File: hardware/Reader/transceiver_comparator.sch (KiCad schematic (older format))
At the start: 12 parts

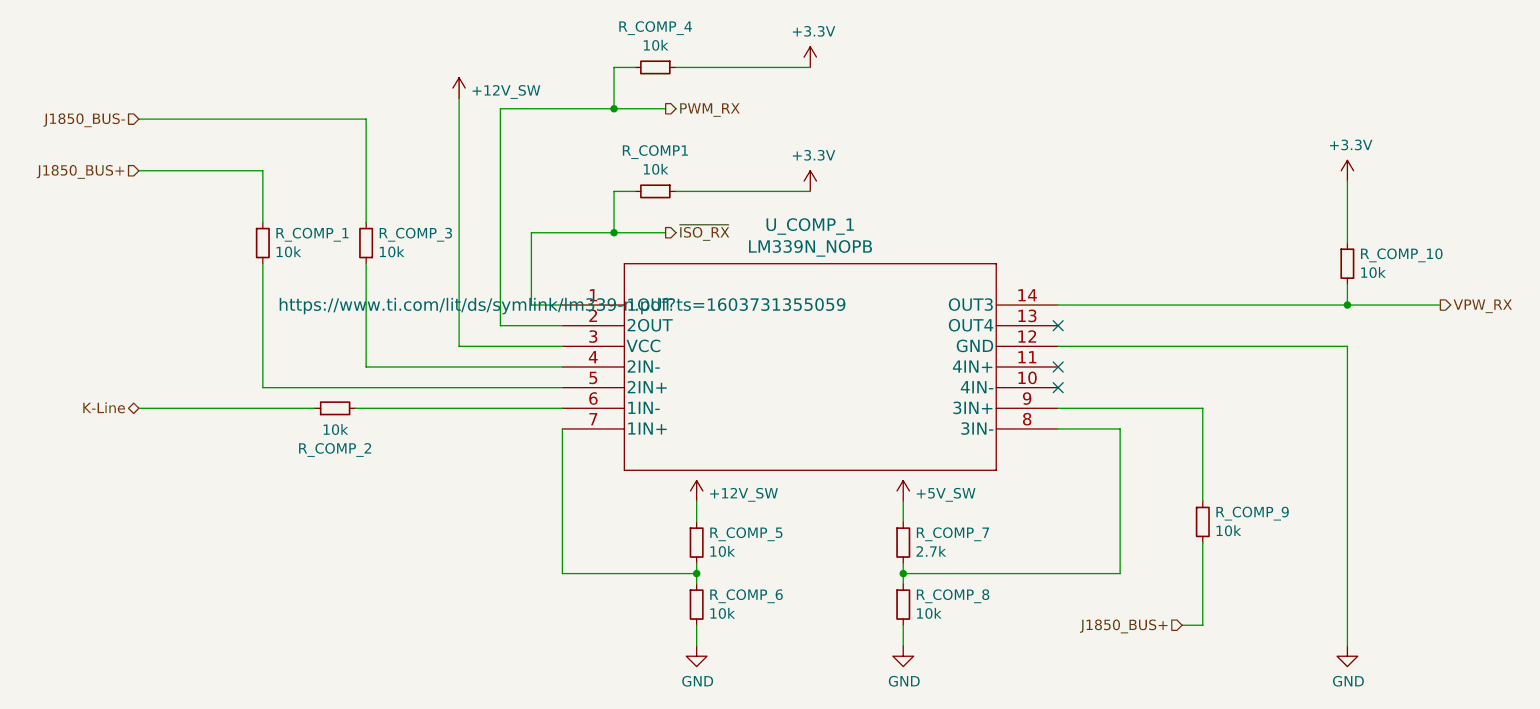
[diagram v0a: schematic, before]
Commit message: Updated reader schematic to v0.0.5 by adding ESP32, removing unused transceivers, fixed design flaws, increased header pins and fixed footprints. Working on reader PCB design
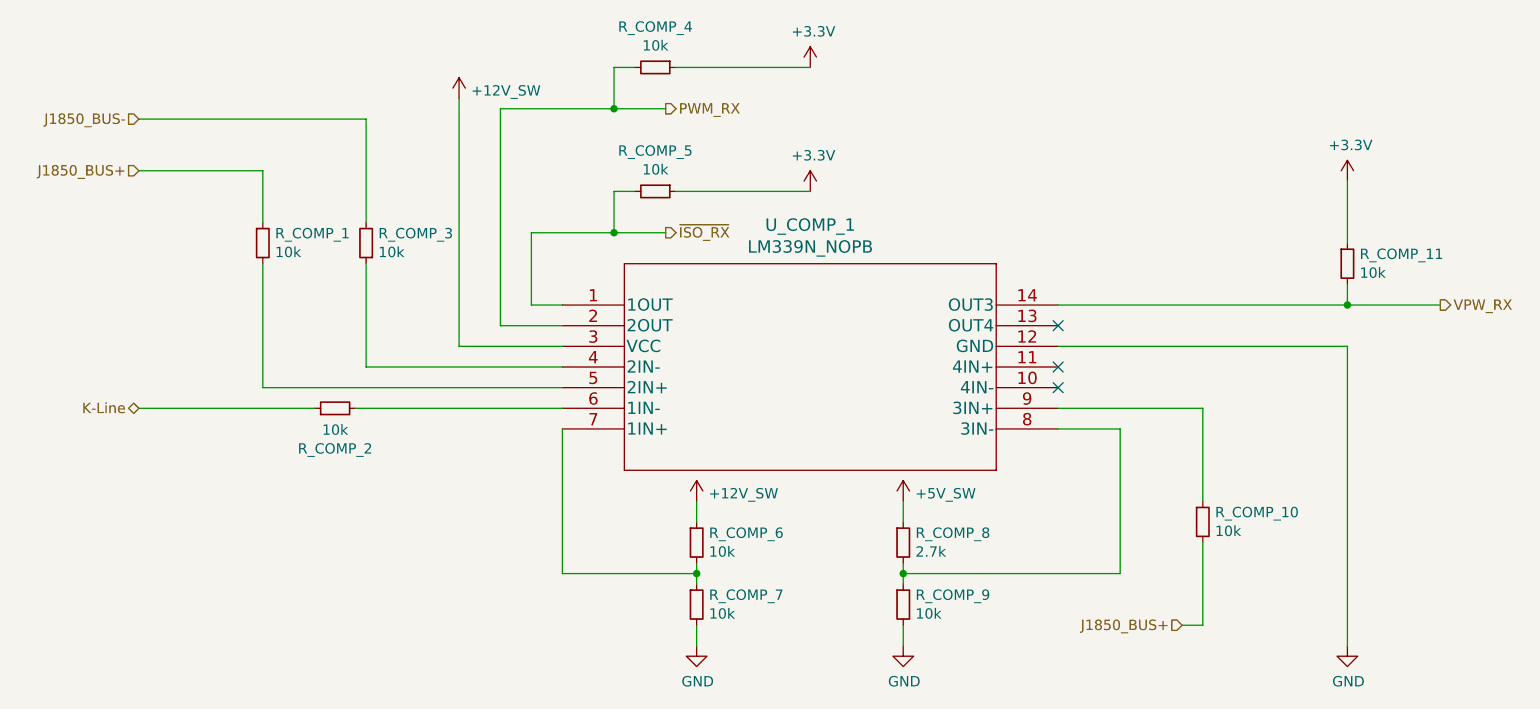
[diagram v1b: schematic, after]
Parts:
- renumbered R_COMP_9 to R_COMP_10, R_COMP_10 to R_COMP_11, R_COMP1 to R_COMP_5, R_COMP_5 to R_COMP_6, R_COMP_6 to R_COMP_7, R_COMP_7 to R_COMP_8, R_COMP_8 to R_COMP_9
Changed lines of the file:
@@
 $Descr USLetter 11000 8500
 encoding utf-8
-Sheet 8 19
+Sheet 16 17
 Title "CANnect Reader | Comparative Transceiver"
-Date "2020-11-19"
+Date "2020-11-27"
 Rev "0.0.05"
 Comp "CANtech"
@@
 P 5250 3350
 AR Path="/5F95F80B/5FA83833/5FB4E408" Ref="R_COMP_?"  Part="1"
-AR Path="/5F95F80B/5FB4CA84/5FB4E408" Ref="R_COMP_5"  Part="1"
-F 0 "R_COMP_5" H 5309 3396 50  0000 L CNN
+AR Path="/5F95F80B/5FB4CA84/5FB4E408" Ref="R_COMP_6"  Part="1"
+F 0 "R_COMP_6" H 5309 3396 50  0000 L CNN
 F 1 "10k" H 5309 3305 50  0000 L CNN
 F 2 "footprints:RESC1608X55N" H 5250 3350 50  0001 C CNN
@@
 P 5250 3650
 AR Path="/5F95F80B/5FA83833/5FB4E431" Ref="R_COMP_?"  Part="1"
-AR Path="/5F95F80B/5FB4CA84/5FB4E431" Ref="R_COMP_6"  Part="1"
-F 0 "R_COMP_6" H 5309 3696 50  0000 L CNN
+AR Path="/5F95F80B/5FB4CA84/5FB4E431" Ref="R_COMP_7"  Part="1"
+F 0 "R_COMP_7" H 5309 3696 50  0000 L CNN
 F 1 "10k" H 5309 3605 50  0000 L CNN
 F 2 "footprints:RESC1608X55N" H 5250 3650 50  0001 C CNN
@@
 $EndComp
 $Comp
-L Device:R_Small R_COMP1
+L Device:R_Small R_COMP_5
 U 1 1 5FBAA6D5
 P 5050 1650
-F 0 "R_COMP1" V 4854 1650 50  0000 C CNN
+F 0 "R_COMP_5" V 4854 1650 50  0000 C CNN
 F 1 "10k" V 4945 1650 50  0000 C CNN
 F 2 "footprints:RESC1608X55N" H 5050 1650 50  0001 C CNN
@@
 J1850_BUS+
 $Comp
-L Device:R_Small R_COMP_9
+L Device:R_Small R_COMP_10
 U 1 1 5FBAD28A
 P 7700 3250
-F 0 "R_COMP_9" H 7759 3296 50  0000 L CNN
+F 0 "R_COMP_10" H 7759 3296 50  0000 L CNN
 F 1 "10k" H 7759 3205 50  0000 L CNN
 F 2 "footprints:RESC1608X55N" H 7700 3250 50  0001 C CNN
@@
 	7700 2700 7700 3150
 $Comp
-L Device:R_Small R_COMP_7
+L Device:R_Small R_COMP_8
 U 1 1 5FBB49DF
 P 6250 3350
-F 0 "R_COMP_7" H 6309 3396 50  0000 L CNN
+F 0 "R_COMP_8" H 6309 3396 50  0000 L CNN
 F 1 "2.7k" H 6309 3305 50  0000 L CNN
 F 2 "footprints:RESC1608X55N" H 6250 3350 50  0001 C CNN
@@
 $EndComp
 $Comp
-L Device:R_Small R_COMP_8
+L Device:R_Small R_COMP_9
 U 1 1 5FBB4DBB
 P 6250 3650
-F 0 "R_COMP_8" H 6309 3696 50  0000 L CNN
+F 0 "R_COMP_9" H 6309 3696 50  0000 L CNN
 F 1 "10k" H 6309 3605 50  0000 L CNN
 F 2 "footprints:RESC1608X55N" H 6250 3650 50  0001 C CNN
@@
 F 1 "LM339N_NOPB" H 5800 2481 60  0000 C CNN
 F 2 "footprints:LM339N&slash_NOPB" H 5800 2440 60  0001 C CNN
-F 3 "https://www.ti.com/lit/ds/symlink/lm339-n.pdf?ts=1603731355059" H 4600 2200 60  0000 C CNN
+F 3 "https://www.ti.com/lit/ds/symlink/lm339-n.pdf?ts=1603731355059" H 4600 2200 60  0001 C CNN
 F 4 "LM339N_NOPB" H 4600 2200 50  0001 C CNN "Part Name"
 F 5 "Texas Instruments" H 4600 2200 50  0001 C CNN "Manufacturer"
@@
 NoConn ~ 7000 2300
 $Comp
-L Device:R_Small R_COMP_10
+L Device:R_Small R_COMP_11
 U 1 1 5FBC1B65
 P 8400 2000
-F 0 "R_COMP_10" H 8459 2046 50  0000 L CNN
+F 0 "R_COMP_11" H 8459 2046 50  0000 L CNN
 F 1 "10k" H 8459 1955 50  0000 L CNN
 F 2 "footprints:RESC1608X55N" H 8400 2000 50  0001 C CNN
